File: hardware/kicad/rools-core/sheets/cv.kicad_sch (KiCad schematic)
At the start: 56 parts, among them U4 OPA4171, U5 MCP6004, U6 LM4040DBZ-10, U9 DAC8565

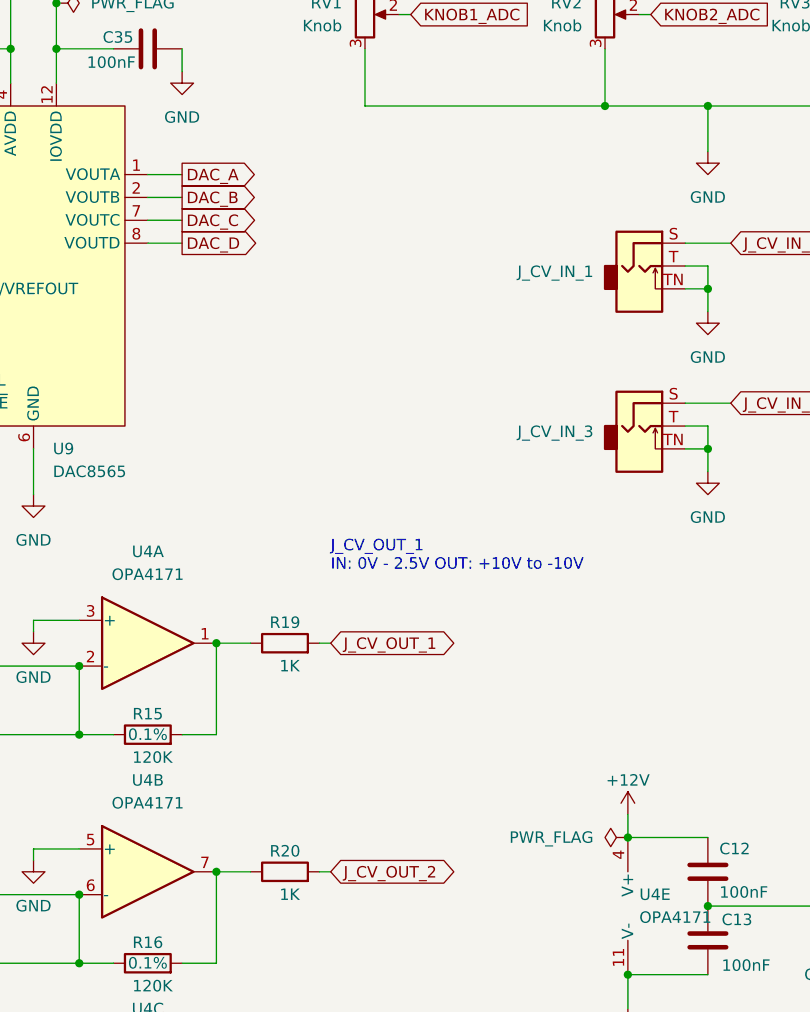
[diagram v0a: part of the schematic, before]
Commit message: Remove Patch reference assets and continue Core PCB routing.
Drop imported Patch symbols, local display footprint, and stale BOM CSV while advancing layout and schematic interconnects.

Co-authored-by: Cursor <cursoragent@cursor.com>
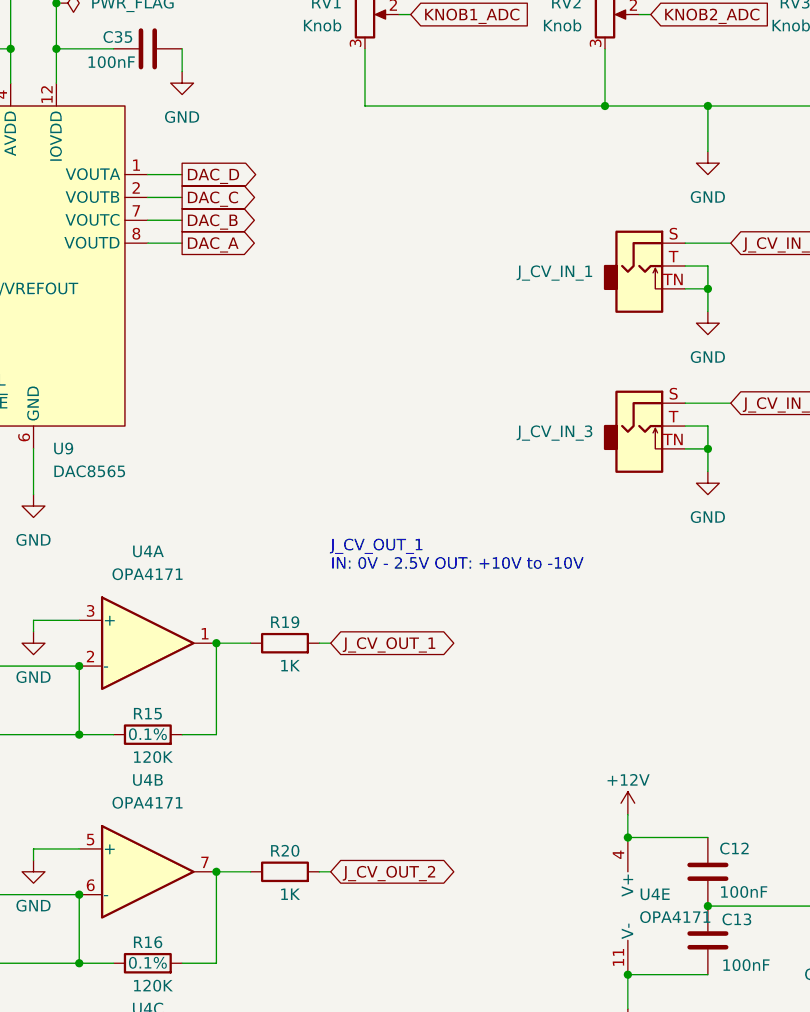
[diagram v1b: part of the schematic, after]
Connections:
- net DAC_A: now also U9.8 (VOUTD); no longer U9.1 (VOUTA)
- net DAC_B: now also U9.7 (VOUTC); no longer U9.2 (VOUTB)
- net DAC_C: now also U9.2 (VOUTB); no longer U9.7 (VOUTC)
- net DAC_D: now also U9.1 (VOUTA); no longer U9.8 (VOUTD)
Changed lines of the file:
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@@
 	(global_label "DAC_B"
 		(shape output)
-		(at 67.31 53.34 0)
+		(at 67.31 55.88 0)
 		(fields_autoplaced yes)
 		(effects
@@
 		)
 		(property "Intersheetrefs" "${INTERSHEET_REFS}"
-			(at 76.2565 53.34 0)
+			(at 76.2565 55.88 0)
 			(hide yes)
 			(show_name no)
@@
 	(global_label "DAC_A"
 		(shape output)
-		(at 67.31 50.8 0)
+		(at 67.31 58.42 0)
 		(fields_autoplaced yes)
 		(effects
@@
 		)
 		(property "Intersheetrefs" "${INTERSHEET_REFS}"
-			(at 76.0751 50.8 0)
+			(at 76.0751 58.42 0)
 			(hide yes)
 			(show_name no)
@@
 	(global_label "DAC_D"
 		(shape output)
-		(at 67.31 58.42 0)
+		(at 67.31 50.8 0)
 		(fields_autoplaced yes)
 		(effects
@@
 		)
 		(property "Intersheetrefs" "${INTERSHEET_REFS}"
-			(at 76.2565 58.42 0)
+			(at 76.2565 50.8 0)
 			(hide yes)
 			(show_name no)
@@
 	(global_label "DAC_C"
 		(shape output)
-		(at 67.31 55.88 0)
+		(at 67.31 53.34 0)
 		(fields_autoplaced yes)
 		(effects
@@
 		)
 		(property "Intersheetrefs" "${INTERSHEET_REFS}"
-			(at 76.2565 55.88 0)
+			(at 76.2565 53.34 0)
 			(hide yes)
 			(show_name no)
@@
 				)
 			)
-		)
-	)
-	(symbol
-		(lib_id "power:PWR_FLAG")
-		(at 116.84 124.46 90)
-		(mirror x)
-		(unit 1)
-		(body_style 1)
-		(exclude_from_sim no)
-		(in_bom yes)
-		(on_board yes)
-		(in_pos_files yes)
-		(dnp no)
-		(property "Reference" "#FLG08"
-			(at 114.935 124.46 0)
-			(hide yes)
-			(show_name no)
-			(do_not_autoplace no)
-			(effects
-				(font
-					(size 1.27 1.27)
-				)
-			)
-		)
-		(property "Value" "PWR_FLAG"
-			(at 113.03 124.4599 90)
-			(show_name no)
-			(do_not_autoplace no)
-			(effects
-				(font
-					(size 1.27 1.27)
-				)
-				(justify left)
-			)
-		)
-		(property "Footprint" ""
-			(at 116.84 124.46 0)
-			(hide yes)
-			(show_name no)
-			(do_not_autoplace no)
-			(effects
-				(font
-					(size 1.27 1.27)
-				)
-			)
-		)
-		(property "Datasheet" ""
-			(at 116.84 124.46 0)
-			(hide yes)
-			(show_name no)
-			(do_not_autoplace no)
-			(effects
-				(font
-					(size 1.27 1.27)
-				)
-			)
-		)
-		(property "Description" "Special symbol for telling ERC where power comes from"
-			(at 116.84 124.46 0)
-			(hide yes)
-			(show_name no)
-			(do_not_autoplace no)
-			(effects
-				(font
-					(size 1.27 1.27)
-				)
-			)
-		)
-		(pin "1"
-		)
-		(instances
-			(project "rools-core"
-				(path "/e63e39d7-6ac0-4ffd-8aa3-1841a4541b55/ca71e2c3-ddd5-4a27-ab61-3d1f14e38d31"
-					(reference "#FLG08")
-					(unit 1)
-				)
-			)
